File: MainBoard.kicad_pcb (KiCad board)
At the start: 2 copper layers, 120 x 68 mm, 79 parts, among them J1 DB25, P1 BOOT, P10 CONN_01X03, P11 CONN_01X03, P12 CONN_01X03, P13 CONN_01X03, P14 CONN_01X02, P15 CONN_02X07, P16 CONN_02X05, P17 CONN_01X04, P18 CONN_01X03, P2 CONN_01X04, P3 CONN_01X05, P4 HOLE, P5 HOLE, P6 HOLE, P7 HOLE, P8 CONN_01X02, P9 CONN_01X03, Q1 BSS138, Q2 BSS138, Q3 DMN65D8L, SW1 RESET, U1 mp2307, U10 SI4425DDY, U2 DYS_mini_ESC, U3 DYS_mini_ESC, U4 DYS_mini_ESC, U5 DYS_mini_ESC, U6 TLV1117LV33, U7 TENDA_P200, U8 pca9685, U9 STM32F103CBT6, Y1 8MHz

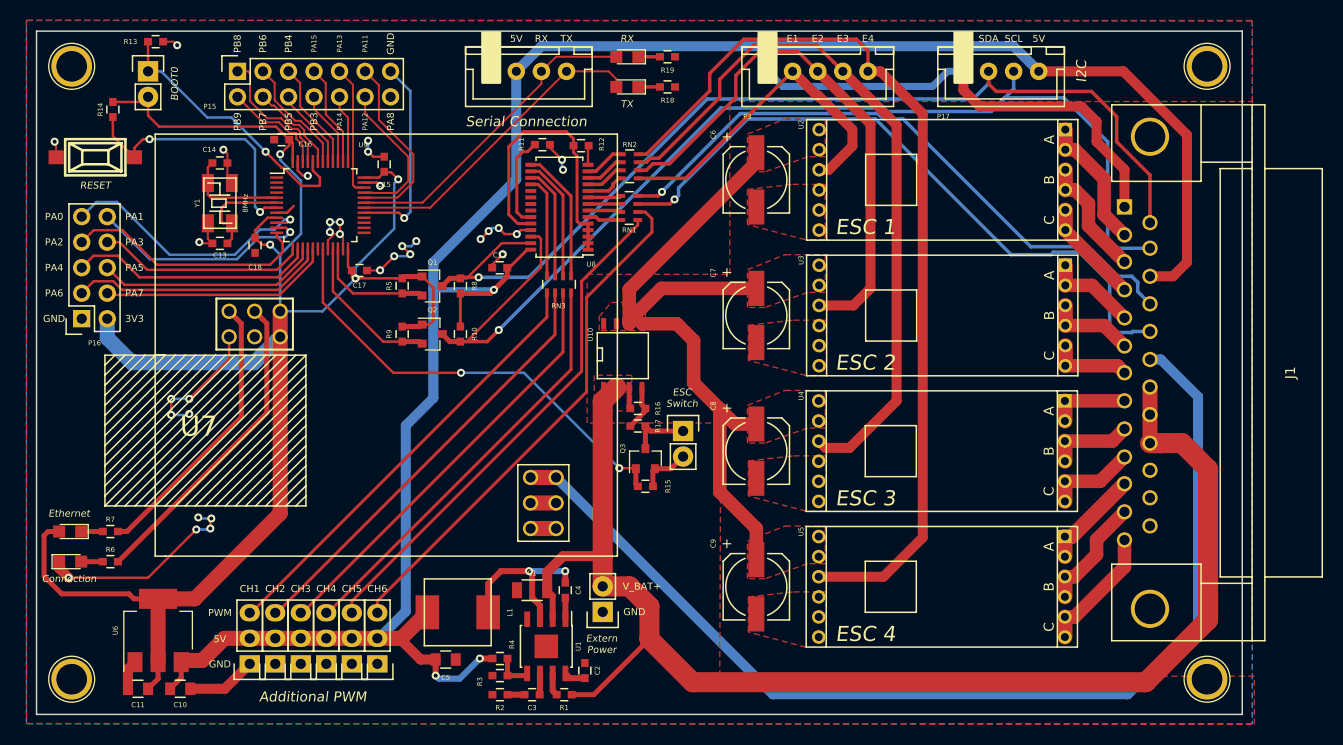
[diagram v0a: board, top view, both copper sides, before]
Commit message: Change db25 footprint
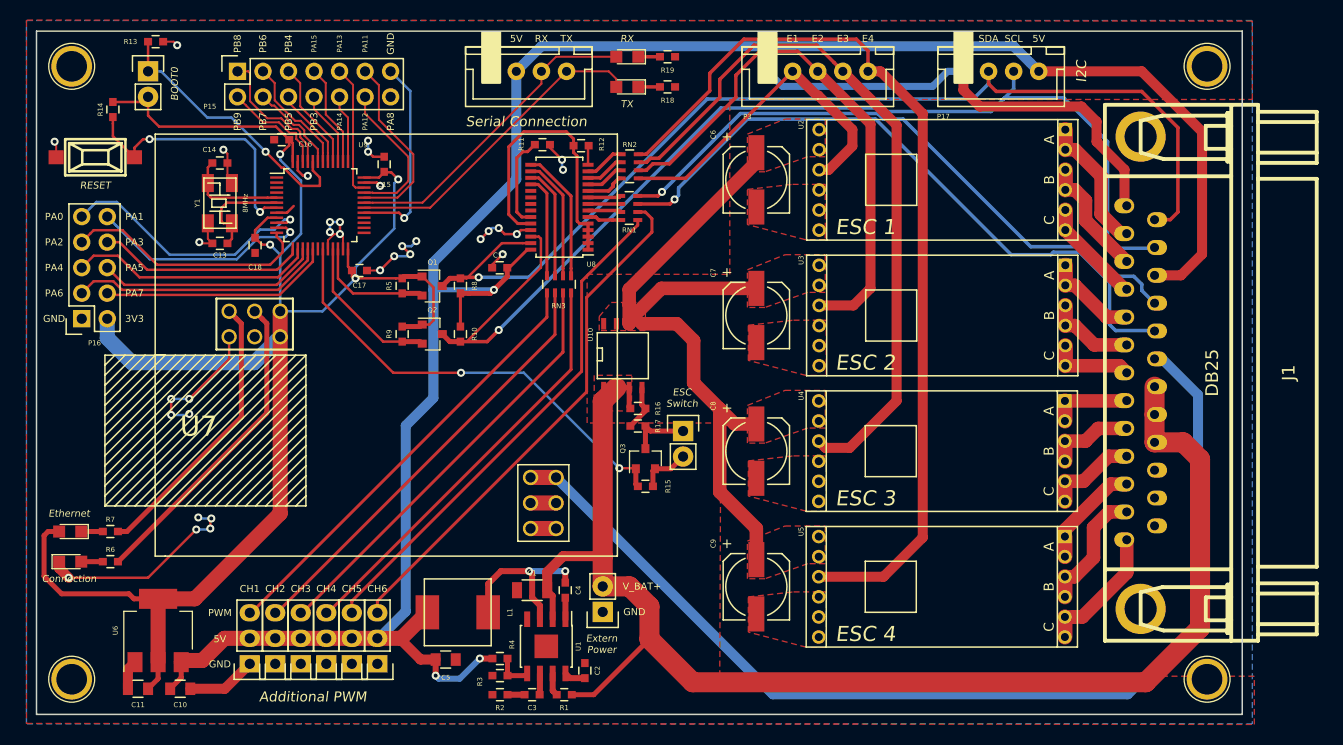
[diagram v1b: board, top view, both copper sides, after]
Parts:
- C12: value C -> 10uF
- C6, C7, C8, C9: value CP1 -> 100uF
- J1: footprint Connect:DB25FC -> footprint:DB_25M
- moved J1 7.45 mm to (197.0, 84.0), turned to 90 degrees
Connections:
- J1 pad 1: GND -> /MOTOR_4C
- J1 pad 10: /MOTOR_3C -> /MOTOR_1C
- J1 pad 11: /MOTOR_4A -> /MOTOR_1B
- J1 pad 12: /MOTOR_4B -> /MOTOR_1A
- J1 pad 13: /MOTOR_4C -> GND
- J1 pad 14: /SDA_5V -> GND
- J1 pad 15: /SCL_5V -> GND
- J1 pad 16: /5V -> GND
- J1 pad 17: /LED2 -> /V_BAT
- J1 pad 18: /LED1 -> /V_BAT
- J1 pad 19: /T+ -> /V_BAT
- J1 pad 2: /MOTOR_1A -> /MOTOR_4B
- J1 pad 20: /V_BAT -> /T+
- J1 pad 21: /V_BAT -> /LED1
- J1 pad 22: /V_BAT -> /LED2
- J1 pad 23: GND -> /5V
- J1 pad 24: GND -> /SCL_5V
- J1 pad 25: GND -> /SDA_5V
- J1 pad 3: /MOTOR_1B -> /MOTOR_4A
- J1 pad 4: /MOTOR_1C -> /MOTOR_3C
- J1 pad 5: /MOTOR_2A -> /MOTOR_3B
- J1 pad 6: /MOTOR_2B -> /MOTOR_3A
- J1 pad 8: /MOTOR_3A -> /MOTOR_2B
- J1 pad 9: /MOTOR_3B -> /MOTOR_2A
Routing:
- net /SDA_5V: track 99.7 -> 105.3 mm
- net /5V: track 211.5 -> 213.8 mm
- net /MOTOR_4B: track 11.5 -> 12.6 mm
- net /V_BAT: track 142.3 -> 141.2 mm
- net /MOTOR_4A: track 10.1 -> 10.7 mm
- net /MOTOR_4C: track 12.7 -> 13.3 mm
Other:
- net class Default: trace_width 0.25 -> 0.35

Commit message: pull up rx/tx indicate led & change esc capacitor size
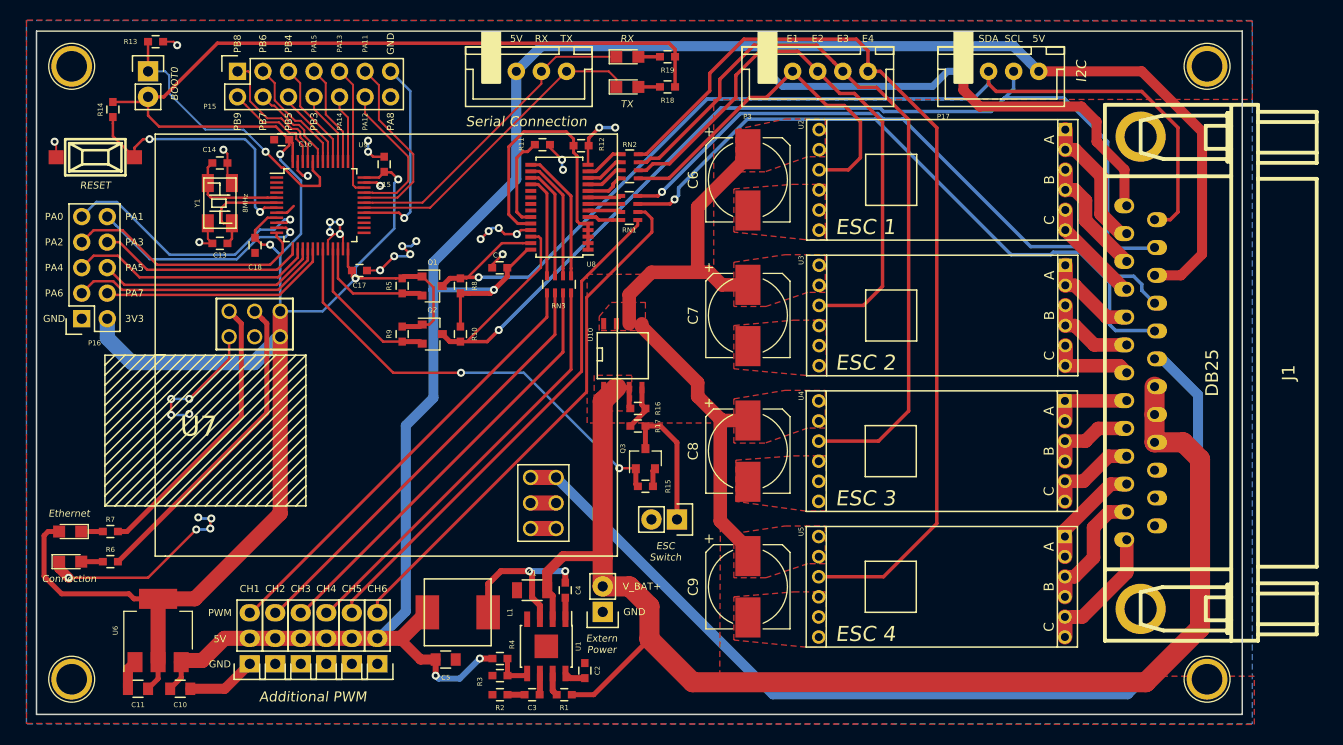
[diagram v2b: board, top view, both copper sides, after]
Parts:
- C6, C7, C8, C9: footprint Capacitors_SMD:c_elec_6.3x4.5 -> Capacitors_SMD:CP_Elec_8x10
- moved P14 8.82 mm to (143.7, 98.6), turned to 180 degrees
- moved C6 0.84 mm to (150.8, 64.8)
- moved C7 0.84 mm to (150.8, 78.3)
- moved C8 0.84 mm to (150.8, 91.8)
- moved C9 0.84 mm to (150.8, 105.3)
- turned D3 to 0 degrees
- turned D4 to 0 degrees
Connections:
- D3 pad 1: Net-(D3-Pad1) -> /TX1
- D3 pad 2: /TX1 -> Net-(D3-Pad2)
- D4 pad 1: Net-(D4-Pad1) -> /RX1
- D4 pad 2: /RX1 -> Net-(D4-Pad2)
- R18 pad 1: GND -> /3V3
- R18 pad 2: Net-(D3-Pad1) -> Net-(D3-Pad2)
- R19 pad 1: GND -> /3V3
- R19 pad 2: Net-(D4-Pad1) -> Net-(D4-Pad2)
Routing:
- net /3V3: track 175.5 -> 234.1 mm
- net /V_PWR: track 71.0 -> 60.8 mm
- net Net-(P14-Pad1): track 6.21 -> 13.7 mm
- net /ESC3: track 72.3 -> 75.0 mm
- net /ESC1: track 34.1 -> 36.8 mm
- net /ESC2: track 54.5 -> 56.9 mm
- net Net-(D4-Pad2): track 0.00 -> 2.15 mm
- net Net-(D4-Pad1): track 2.15 -> 0.00 mm
- net Net-(D3-Pad2): track 0.00 -> 2.15 mm
- net Net-(D3-Pad1): track 2.15 -> 0.00 mm
- net /ESC4: track 92.5 -> 93.7 mm
- net Net-(P1-Pad1): track 27.5 -> 28.6 mm
- net GND: track 148.0 -> 148.5 mm, vias 33 -> 35

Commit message: change plc module position
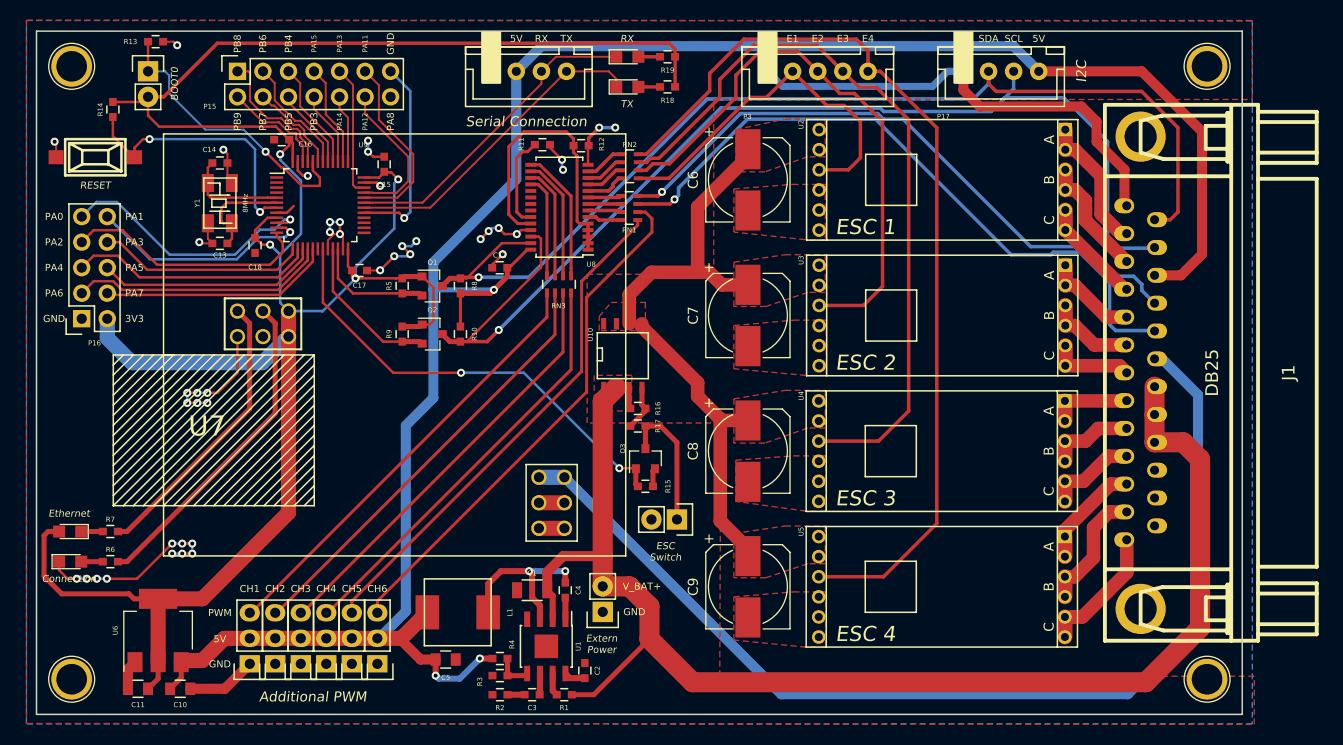
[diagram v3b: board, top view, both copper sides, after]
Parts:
- moved U7 0.83 mm to (116.2, 81.3)
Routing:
- net GND: track 148.5 -> 146.3 mm, vias 35 -> 42
- net /3V3: track 234.1 -> 235.3 mm
- net Net-(R6-Pad1): track 31.6 -> 32.5 mm
- net /T+: track 106.9 -> 106.1 mm
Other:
- net class Default: trace_width 0.35 -> 0.25

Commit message: change regulator position
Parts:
- moved P8 9.67 mm to (144.5, 113.0), turned to 0 degrees
- moved C1 5.00 mm to (134.3, 105.6)
- moved C2 5.00 mm to (139.6, 113.6)
- moved C3 5.00 mm to (134.3, 116.0)
- moved C4 5.00 mm to (137.6, 105.6)
- moved C5 5.00 mm to (125.7, 112.5)
- moved L1 5.00 mm to (126.9, 107.8)
- moved R1 5.00 mm to (137.5, 116.0)
- moved R2 5.00 mm to (131.1, 116.0)
- moved R3 5.00 mm to (131.1, 114.1)
- moved R4 5.00 mm to (131.1, 112.4)
- moved U1 5.00 mm to (135.7, 111.2)
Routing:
- net /5V: track 213.8 -> 219.6 mm
- net /V_BAT: track 141.2 -> 137.7 mm
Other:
- net class Default: trace_width 0.25 -> 2

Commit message: v.0.1
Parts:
- added C19: 220uF/10V, Capacitors_SMD:CP_Elec_6.3x5.8, F.Cu at (98.5, 111.6)
- P16: value CONN_02X05 -> CONN_02X04; footprint Socket_Strips:Socket_Strip_Straight_2x05 -> Socket_Strips:Socket_Strip_Straight_2x04
- P3: value CONN_01X05 -> CONN_02X04; footprint Connectors_JST:JST_XH_B05B-XH-A_05x2.50mm_Straight -> Socket_Strips:Socket_Strip_Straight_2x04
- moved R16 40.5 mm to (173.1, 110.7), turned to 90 degrees
- moved RN2 38.9 mm to (120.4, 97.6), turned to 90 degrees
- moved U10 38.8 mm to (167.2, 108.3)
- moved R12 38.6 mm to (111.4, 92.6), turned to 90 degrees
- moved R17 38.0 mm to (171.3, 110.7), turned to 90 degrees
- moved RN1 37.8 mm to (116.0, 97.6), turned to 90 degrees
- moved P3 28.1 mm to (143.7, 80.6), turned to 270 degrees
- moved U8 27.1 mm to (117.8, 90.6), turned to 90 degrees
- moved R11 26.8 mm to (125.4, 87.6)
- moved C12 21.5 mm to (111.4, 89.2), turned to 270 degrees
- moved RN3 16.9 mm to (125.4, 90.8), turned to 0 degrees
- moved R10 10.7 mm to (112.0, 83.2), turned to 0 degrees
- moved R8 10.1 mm to (116.0, 83.2), turned to 180 degrees
- moved R13 8.55 mm to (91.8, 59.6)
- moved Q2 7.44 mm to (112.0, 80.4), turned to 270 degrees
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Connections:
- net /OSC_IN renamed /OSC_N
- net /OSC_OUT renamed /OSC_P
- P10 pad 3: /CH2 -> /CH1
- P11 pad 3: /CH3 -> /CH2
- P12 pad 3: /CH4 -> /CH3
- P13 pad 3: /CH5 -> /CH4
- P18 pad 3: /CH6 -> /CH5
- P2 pad 1: GND -> /RX1
- P2 pad 2: /5V -> /TX1
- P2 pad 3: /RX1 -> /5V
- P2 pad 4: /TX1 -> GND
- P3 pad 1: GND -> /ESC1
- P3 pad 2: /ESC1 -> /CH10
- P3 pad 4: /ESC3 -> /CH11
- P3 pad 5: /ESC4 -> /ESC3
- P4 pad 1: (no net) -> Net-(P4-Pad1)
- P5 pad 1: (no net) -> Net-(P5-Pad1)
- P6 pad 1: (no net) -> Net-(P6-Pad1)
- P7 pad 1: (no net) -> Net-(P7-Pad1)
- P9 pad 3: /CH1 -> /CH0
- RN1 pad 1: /CH5 -> /CH0
- RN1 pad 2: /CH6 -> /CH1
- RN1 pad 3: /LED1 -> /CH2
- RN1 pad 4: /LED2 -> /CH3
- RN2 pad 1: /ESC1 -> /CH4
- RN2 pad 2: /ESC2 -> /CH5
- RN2 pad 3: /ESC3 -> /CH6
- RN2 pad 4: /ESC4 -> /CH7
- RN3 pad 5: /CH1 -> /CH11
- RN3 pad 6: /CH2 -> /CH10
- RN3 pad 7: /CH3 -> /LED1
- RN3 pad 8: /CH4 -> /LED2
- U7 pad P: (no net) -> Net-(U7-PadP)
- U8 pad 19: (no net) -> Net-(U8-Pad19)
- U8 pad 20: (no net) -> Net-(U8-Pad20)
- U8 pad 21: (no net) -> Net-(U8-Pad21)
- U8 pad 22: (no net) -> Net-(U8-Pad22)
- U9 pad 1: (no net) -> Net-(U9-Pad1)
- U9 pad 18: (no net) -> Net-(U9-Pad18)
- U9 pad 19: /PWR_SW -> /PB1
- U9 pad 2: (no net) -> Net-(U9-Pad2)
- U9 pad 25: (no net) -> /PWR_SW
- U9 pad 26: (no net) -> /PB13
- U9 pad 27: (no net) -> /PB14
- U9 pad 28: (no net) -> /PB15
- U9 pad 3: (no net) -> Net-(U9-Pad3)
- U9 pad 4: (no net) -> Net-(U9-Pad4)
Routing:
- net /SCL_5V: track 111.8 -> 38.9 mm, vias 1 -> 2
- net /5V: track 219.6 -> 152.9 mm, vias 3 -> 2
- net GND: track 146.3 -> 80.9 mm, vias 42 -> 13
- net /ESC4: track 93.7 -> 28.6 mm
- net /SDA_5V: track 105.3 -> 40.5 mm, vias 1 -> 0
- net /V_PWR: track 60.8 -> 1.50 mm
- net /ESC3: track 75.0 -> 17.1 mm
- net /V_BAT: track 137.7 -> 90.7 mm
- net /PWR_SW: track 45.2 -> 2.08 mm, vias 2 -> 0
- net /CH5: track 50.9 -> 10.3 mm
- net /ESC2: track 56.9 -> 16.6 mm
- net /LED2: track 63.0 -> 97.1 mm
- net /LED1: track 66.8 -> 99.6 mm
- net /CH1: track 44.2 -> 12.7 mm
- net /CH3: track 42.7 -> 11.2 mm
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- removed copper zone on F.Cu, net /V_BAT
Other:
- net class Default: trace_width 2 -> 0.3
- board text removed: "E1"
- board text removed: "E2"
- board text removed: "E3"
- board text removed: "E4"
- board text removed: "PA0"
- board text removed: "PA1"

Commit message: routing...
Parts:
- removed P17: CONN_01X04, Connectors_JST:JST_XH_B04B-XH-A_04x2.50mm_Straight
- removed R12: 10k, Capacitors_SMD:C_0603
- added C21: 22uF/10V, Capacitors_SMD:C_0805, F.Cu at (125.8, 114.8)
- C6, C7, C8, C9: value 100uF -> 220uF/25V
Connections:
- J1 pad 23: /5V -> /3V3
- J1 pad 24: /SCL_5V -> /SCL_3V3
- J1 pad 25: /SDA_5V -> /SDA_3V3
- U8 pad 1: Net-(R12-Pad1) -> GND
- U8 pad 2: Net-(R12-Pad1) -> GND
- U8 pad 24: Net-(R12-Pad1) -> GND
- U8 pad 3: Net-(R12-Pad1) -> GND
- U8 pad 4: Net-(R12-Pad1) -> GND
- U8 pad 5: Net-(R12-Pad1) -> GND
- U9 pad 19: /PB1 -> /PWR_SW
- U9 pad 25: /PWR_SW -> /PB12
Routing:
- net /SCL_3V3: track 8.53 -> 130.0 mm, vias 0 -> 2
- net /SDA_3V3: track 11.9 -> 123.4 mm
- net /3V3: track 255.0 -> 326.9 mm
- net /PWR_SW: track 2.08 -> 54.3 mm, vias 0 -> 2
- net Net-(P14-Pad1): track 4.36 -> 46.3 mm
- net /SDA_5V: track 40.5 -> 7.54 mm
- net /SCL_5V: track 38.9 -> 8.55 mm
- net GND: track 80.9 -> 50.6 mm, vias 13 -> 12
- net /5V: track 152.9 -> 137.5 mm, vias 2 -> 5
- net Net-(R12-Pad1): track 10.5 -> 0.00 mm
- net Net-(R16-Pad2): track 0.00 -> 5.29 mm
- net /PA8: track 19.0 -> 22.8 mm
- net /V_BAT: track 90.7 -> 93.0 mm
- net /CH6: track 26.3 -> 28.4 mm
- net /CH7: track 24.9 -> 26.9 mm
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- added copper zone on F.Cu, net /5V
- added copper zone on F.Cu, net /V_BAT
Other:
- net class Default: trace_width 0.3 -> 0.2
- board text added: "ESC PWM"
- board text added: "SDA 3V3"
- board text removed: "I2C"
- board text removed: "SCL"
- board text removed: "SDA"
- board text removed: "SDA 5V"

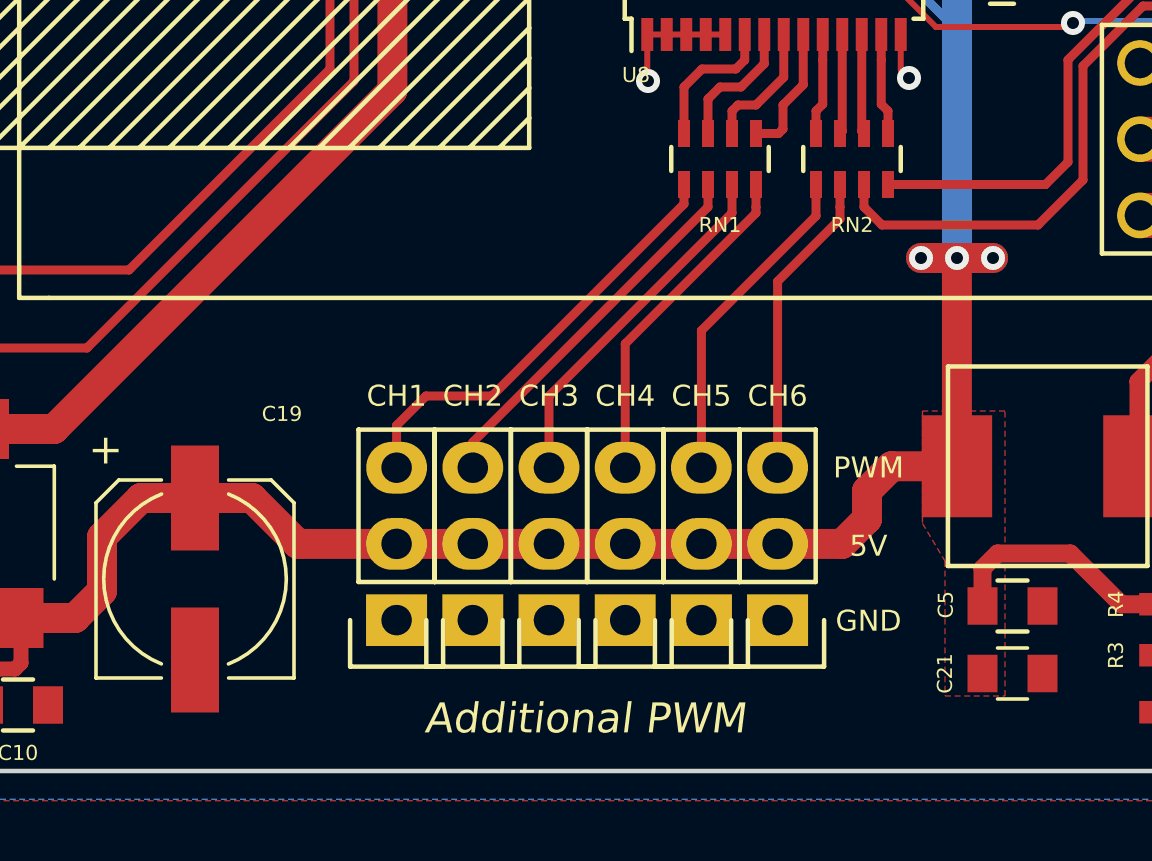
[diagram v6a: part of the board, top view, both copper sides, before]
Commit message: move pwm pin position
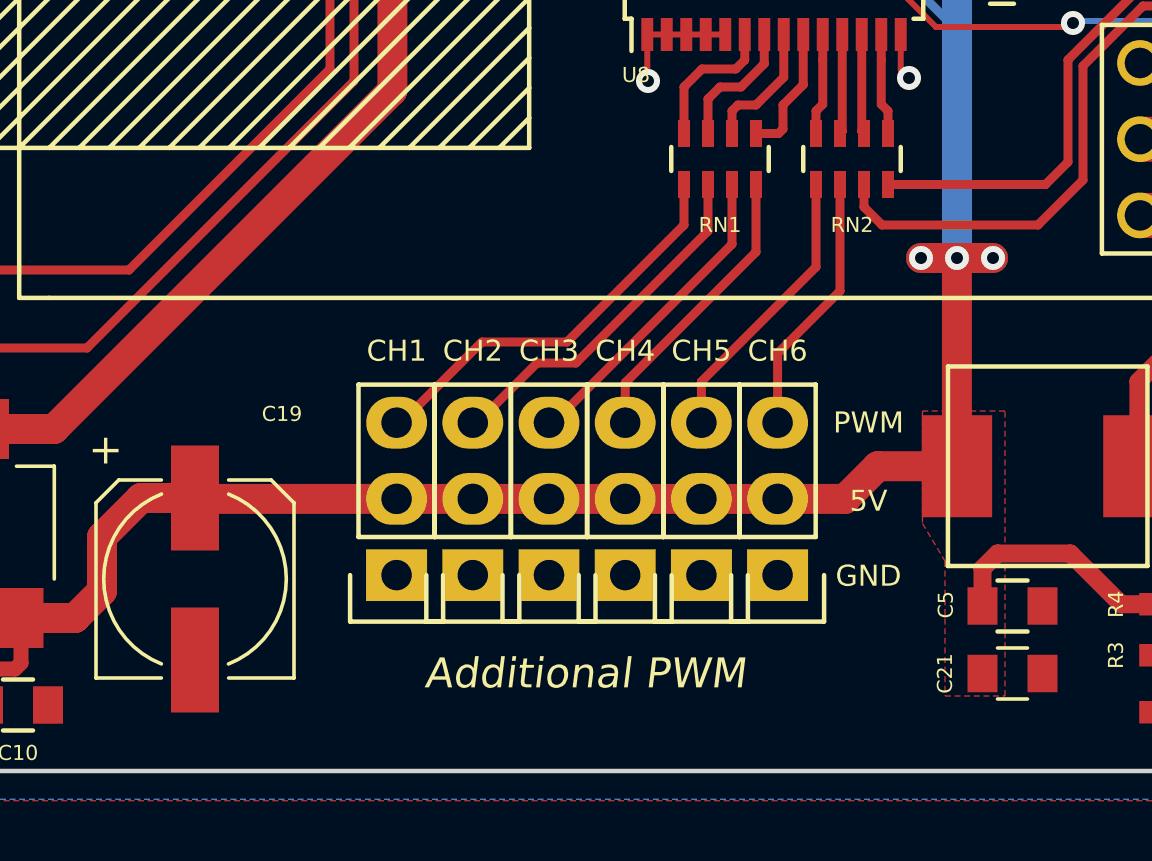
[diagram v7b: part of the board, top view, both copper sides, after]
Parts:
- moved P10 1.50 mm to (107.8, 111.5)
- moved P11 1.50 mm to (110.3, 111.5)
- moved P12 1.50 mm to (112.8, 111.5)
- moved P13 1.50 mm to (115.4, 111.5)
- moved P18 1.50 mm to (117.9, 111.5)
- moved P9 1.50 mm to (105.2, 111.5)
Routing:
- net /5V: track 137.5 -> 135.7 mm
- net /CH4: track 11.0 -> 9.52 mm
- net /CH3: track 11.2 -> 9.75 mm
- net /CH5: track 10.3 -> 8.80 mm
- net /CH2: track 12.0 -> 10.6 mm
- net /CH0: track 14.7 -> 13.7 mm
- net /CH1: track 12.7 -> 12.0 mm
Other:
- net class Default: trace_width 0.2 -> 0.3
